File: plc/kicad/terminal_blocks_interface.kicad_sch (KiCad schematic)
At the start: 78 parts, among them CN1 DB128V-5.08-2P-GN-S, CN10 DB128V-5.08-6P-GN-S, CN2 DB128V-5.08-2P-GN-S, CN3 DB128V-5.08-2P-GN-S, CN4 DB128V-5.08-2P-GN-S, CN5 DB128V-5.08-2P-GN-S, CN6 DB128V-5.08-2P-GN-S, CN7 DB128V-5.08-2P-GN-S, CN8 DB128V-5.08-2P-GN-S, CN9 DB128V-5.08-2P-GN-S, Q1 AO3400A, Q2 AO3400A, U1 TCA9535PWR, U2 TPS272C45DRHFR, U3 TPS272C45DRHFR, U4 ADS1115IDGSR, U5 LTV-814S-TA1-A, U6 LTV-814S-TA1-A, U7 LTV-814S-TA1-A, U8 LTV-814S-TA1-A

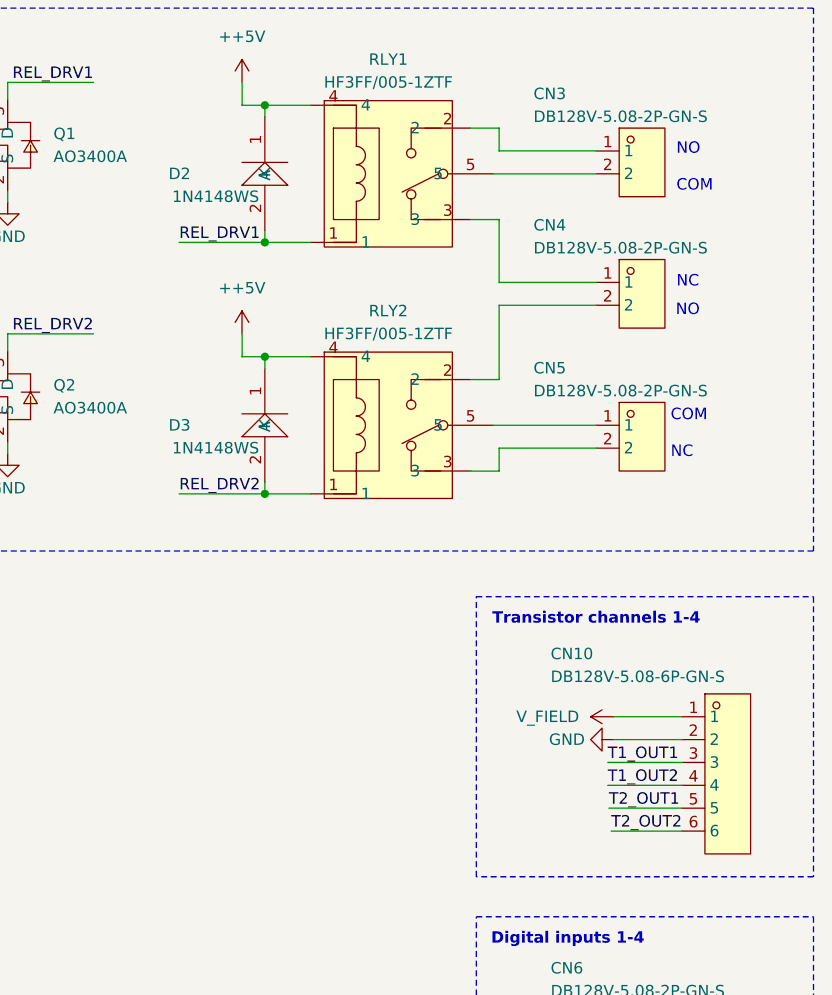
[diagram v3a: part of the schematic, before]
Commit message: Rearranged small PCB placements
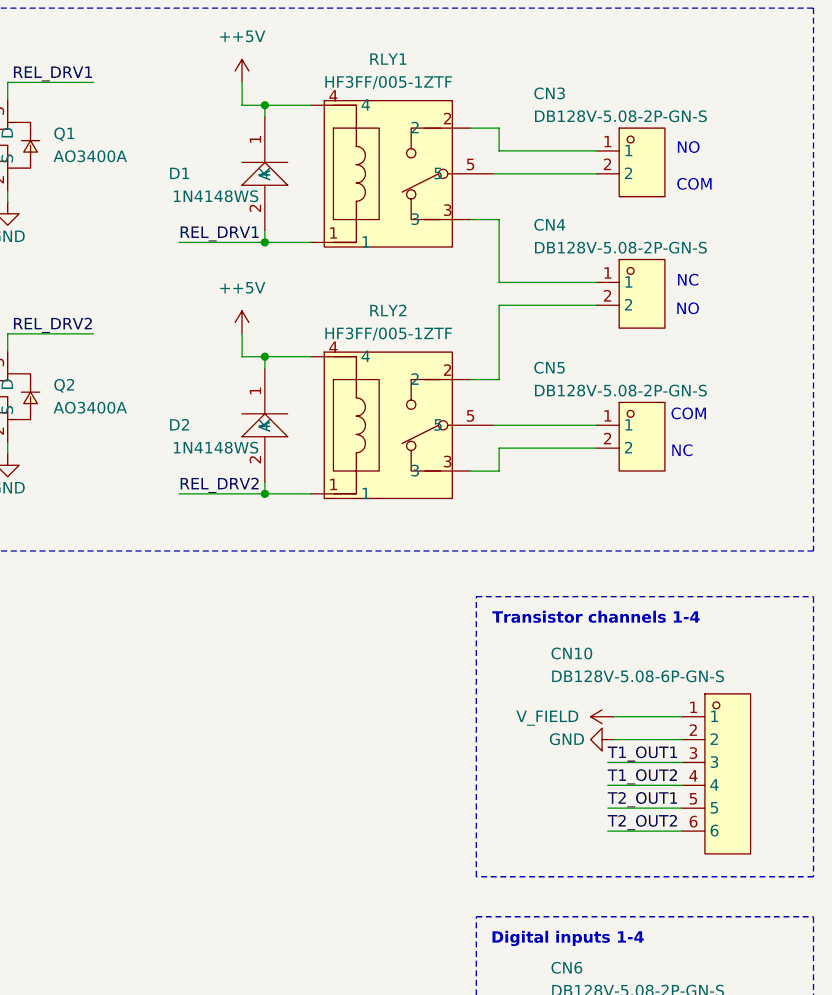
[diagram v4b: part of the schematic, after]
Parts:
- renumbered D2 to D1, D3 to D2
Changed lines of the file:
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@@
 	(wire
 		(pts
-			(xy 376.936 110.49) (xy 384.81 110.49)
+			(xy 376.555 110.49) (xy 384.81 110.49)
 		)
 		(stroke
@@
 	(wire
 		(pts
-			(xy 376.682 107.95) (xy 384.81 107.95)
+			(xy 376.555 107.95) (xy 384.81 107.95)
 		)
 		(stroke
@@
 	)
 	(label "T2_OUT2"
-		(at 376.936 110.49 0)
+		(at 376.555 110.49 0)
 		(effects
 			(font
@@
 	)
 	(label "T2_OUT1"
-		(at 376.682 107.95 0)
+		(at 376.555 107.95 0)
 		(effects
 			(font
@@
 		(in_pos_files yes)
 		(dnp no)
-		(property "Reference" "#PWR068"
+		(property "Reference" "#PWR066"
 			(at 377.19 213.36 0)
 			(hide yes)
@@
 			(project "LibrePLC32"
 				(path "/ef4c1a27-85a3-413a-9f93-a41c4f97eee5/7299de7e-bdc9-4cc1-ab0f-f2b9af304cf6"
-					(reference "#PWR068")
+					(reference "#PWR066")
 					(unit 1)
 				)
@@
 		(dnp no)
 		(fields_autoplaced yes)
-		(property "Reference" "#PWR064"
+		(property "Reference" "#PWR062"
 			(at 335.915 59.055 0)
 			(hide yes)
@@
 			(project "LibrePLC32"
 				(path "/ef4c1a27-85a3-413a-9f93-a41c4f97eee5/7299de7e-bdc9-4cc1-ab0f-f2b9af304cf6"
-					(reference "#PWR064")
+					(reference "#PWR062")
 					(unit 1)
 				)
@@
 		(in_pos_files yes)
 		(dnp no)
-		(property "Reference" "D2"
+		(property "Reference" "D1"
 			(at 330.2 37.465 90)
 			(show_name no)
@@
 			(project "LibrePLC32"
 				(path "/ef4c1a27-85a3-413a-9f93-a41c4f97eee5/7299de7e-bdc9-4cc1-ab0f-f2b9af304cf6"
-					(reference "D2")
+					(reference "D1")
 					(unit 1)
 				)
@@
 		(in_pos_files yes)
 		(dnp no)
-		(property "Reference" "#PWR061"
+		(property "Reference" "#PWR059"
 			(at 309.88 46.99 0)
 			(hide yes)
@@
 			(project "LibrePLC32"
 				(path "/ef4c1a27-85a3-413a-9f93-a41c4f97eee5/7299de7e-bdc9-4cc1-ab0f-f2b9af304cf6"
-					(reference "#PWR061")
+					(reference "#PWR059")
 					(unit 1)
 				)
@@
 		(dnp no)
 		(fields_autoplaced yes)
-		(property "Reference" "#PWR049"
+		(property "Reference" "#PWR047"
 			(at 130.81 264.795 0)
 			(hide yes)
@@
 			(project "LibrePLC32"
 				(path "/ef4c1a27-85a3-413a-9f93-a41c4f97eee5/7299de7e-bdc9-4cc1-ab0f-f2b9af304cf6"
-					(reference "#PWR049")
+					(reference "#PWR047")
 					(unit 1)
 				)
@@
 		(dnp no)
 		(fields_autoplaced yes)
-		(property "Reference" "#PWR063"
+		(property "Reference" "#PWR061"
 			(at 335.915 31.115 0)
 			(hide yes)
@@
 			(project "LibrePLC32"
 				(path "/ef4c1a27-85a3-413a-9f93-a41c4f97eee5/7299de7e-bdc9-4cc1-ab0f-f2b9af304cf6"
-					(reference "#PWR063")
+					(reference "#PWR061")
 					(unit 1)
 				)
@@
 		(dnp no)
 		(fields_autoplaced yes)
-		(property "Reference" "#PWR048"
+		(property "Reference" "#PWR046"
 			(at 130.81 259.715 0)
 			(hide yes)
@@
 			(project "LibrePLC32"
 				(path "/ef4c1a27-85a3-413a-9f93-a41c4f97eee5/7299de7e-bdc9-4cc1-ab0f-f2b9af304cf6"
-					(reference "#PWR048")
+					(reference "#PWR046")
 					(unit 1)
 				)
@@
 		(in_pos_files yes)
 		(dnp no)
-		(property "Reference" "#PWR052"
+		(property "Reference" "#PWR050"
 			(at 216.027 62.992 0)
 			(hide yes)
@@
 			(project "LibrePLC32"
 				(path "/ef4c1a27-85a3-413a-9f93-a41c4f97eee5/7299de7e-bdc9-4cc1-ab0f-f2b9af304cf6"
-					(reference "#PWR052")
+					(reference "#PWR050")
 					(unit 1)
 				)
@@
 		(in_pos_files yes)
 		(dnp no)
-		(property "Reference" "#PWR055"
+		(property "Reference" "#PWR053"
 			(at 227.457 54.737 0)
 			(hide yes)
@@
 			(project "LibrePLC32"
 				(path "/ef4c1a27-85a3-413a-9f93-a41c4f97eee5/7299de7e-bdc9-4cc1-ab0f-f2b9af304cf6"
-					(reference "#PWR055")
+					(reference "#PWR053")
 					(unit 1)
 				)
@@
 		(dnp no)
 		(fields_autoplaced yes)
-		(property "Reference" "#PWR067"
+		(property "Reference" "#PWR065"
 			(at 370.84 100.33 0)
 			(hide yes)
@@
 			(project "LibrePLC32"
 				(path "/ef4c1a27-85a3-413a-9f93-a41c4f97eee5/7299de7e-bdc9-4cc1-ab0f-f2b9af304cf6"
-					(reference "#PWR067")
+					(reference "#PWR065")
 					(unit 1)
 				)
@@
 		(in_pos_files yes)
 		(dnp no)
-		(property "Reference" "#PWR050"
+		(property "Reference" "#PWR048"
 			(at 175.895 264.795 0)
 			(hide yes)
@@
 			(project "LibrePLC32"
 				(path "/ef4c1a27-85a3-413a-9f93-a41c4f97eee5/7299de7e-bdc9-4cc1-ab0f-f2b9af304cf6"
-					(reference "#PWR050")
+					(reference "#PWR048")
 					(unit 1)
 				)
@@
 		(in_pos_files yes)
 		(dnp no)
-		(property "Reference" "#PWR062"
+		(property "Reference" "#PWR060"
 			(at 309.88 74.93 0)
 			(hide yes)
@@
 			(project "LibrePLC32"
 				(path "/ef4c1a27-85a3-413a-9f93-a41c4f97eee5/7299de7e-bdc9-4cc1-ab0f-f2b9af304cf6"
-					(reference "#PWR062")
+					(reference "#PWR060")
 					(unit 1)
 				)
@@
 		(dnp no)
 		(fields_autoplaced yes)
-		(property "Reference" "#PWR066"
+		(property "Reference" "#PWR064"
 			(at 381 97.79 0)
 			(hide yes)
@@
 			(project "LibrePLC32"
 				(path "/ef4c1a27-85a3-413a-9f93-a41c4f97eee5/7299de7e-bdc9-4cc1-ab0f-f2b9af304cf6"
-					(reference "#PWR066")
+					(reference "#PWR064")
 					(unit 1)
 				)
@@
 		(in_pos_files yes)
 		(dnp no)
-		(property "Reference" "#PWR056"
+		(property "Reference" "#PWR054"
 			(at 227.457 83.947 0)
 			(hide yes)
@@
 			(project "LibrePLC32"
 				(path "/ef4c1a27-85a3-413a-9f93-a41c4f97eee5/7299de7e-bdc9-4cc1-ab0f-f2b9af304cf6"
-					(reference "#PWR056")
+					(reference "#PWR054")
 					(unit 1)
 				)
@@
 		(in_pos_files yes)
 		(dnp no)
-		(property "Reference" "#PWR060"
+		(property "Reference" "#PWR058"
 			(at 299.72 79.375 0)
 			(hide yes)
@@
 			(project "LibrePLC32"
 				(path "/ef4c1a27-85a3-413a-9f93-a41c4f97eee5/7299de7e-bdc9-4cc1-ab0f-f2b9af304cf6"
-					(reference "#PWR060")
+					(reference "#PWR058")
 					(unit 1)
 				)
@@
 		(in_pos_files yes)
 		(dnp no)
-		(property "Reference" "#PWR058"
+		(property "Reference" "#PWR056"
 			(at 227.457 141.732 0)
 			(hide yes)
@@
 			(project "LibrePLC32"
 				(path "/ef4c1a27-85a3-413a-9f93-a41c4f97eee5/7299de7e-bdc9-4cc1-ab0f-f2b9af304cf6"
-					(reference "#PWR058")
+					(reference "#PWR056")
 					(unit 1)
 				)
@@
 		(in_pos_files yes)
 		(dnp no)
-		(property "Reference" "#PWR054"
+		(property "Reference" "#PWR052"
 			(at 216.027 120.777 0)
 			(hide yes)
@@
 			(project "LibrePLC32"
 				(path "/ef4c1a27-85a3-413a-9f93-a41c4f97eee5/7299de7e-bdc9-4cc1-ab0f-f2b9af304cf6"
-					(reference "#PWR054")
+					(reference "#PWR052")
 					(unit 1)
 				)
@@
 		(in_pos_files yes)
 		(dnp no)
-		(property "Reference" "#PWR065"
+		(property "Reference" "#PWR063"
 			(at 348.615 223.52 0)
 			(hide yes)
@@
 			(project "LibrePLC32"
 				(path "/ef4c1a27-85a3-413a-9f93-a41c4f97eee5/7299de7e-bdc9-4cc1-ab0f-f2b9af304cf6"
-					(reference "#PWR065")
+					(reference "#PWR063")
 					(unit 1)
 				)
@@
 		(in_pos_files yes)
 		(dnp no)
-		(property "Reference" "#PWR057"
+		(property "Reference" "#PWR055"
 			(at 227.457 111.887 0)
 			(hide yes)
@@
 			(project "LibrePLC32"
 				(path "/ef4c1a27-85a3-413a-9f93-a41c4f97eee5/7299de7e-bdc9-4cc1-ab0f-f2b9af304cf6"
-					(reference "#PWR057")
+					(reference "#PWR055")
 					(unit 1)
 				)
@@
 		(in_pos_files yes)
 		(dnp no)
-		(property "Reference" "#PWR051"
+		(property "Reference" "#PWR049"
 			(at 216.027 33.782 0)
 			(hide yes)
@@
 			(project "LibrePLC32"
 				(path "/ef4c1a27-85a3-413a-9f93-a41c4f97eee5/7299de7e-bdc9-4cc1-ab0f-f2b9af304cf6"
-					(reference "#PWR051")
+					(reference "#PWR049")
 					(unit 1)
 				)
@@
 		(in_pos_files yes)
 		(dnp no)
-		(property "Reference" "#PWR053"
+		(property "Reference" "#PWR051"
 			(at 216.027 90.932 0)
 			(hide yes)
@@
 			(project "LibrePLC32"
 				(path "/ef4c1a27-85a3-413a-9f93-a41c4f97eee5/7299de7e-bdc9-4cc1-ab0f-f2b9af304cf6"
-					(reference "#PWR053")
+					(reference "#PWR051")
 					(unit 1)
 				)
@@
 		(in_pos_files yes)
 		(dnp no)
-		(property "Reference" "#PWR059"
+		(property "Reference" "#PWR057"
 			(at 299.72 51.435 0)
 			(hide yes)
@@
 			(project "LibrePLC32"
 				(path "/ef4c1a27-85a3-413a-9f93-a41c4f97eee5/7299de7e-bdc9-4cc1-ab0f-f2b9af304cf6"
-					(reference "#PWR059")
+					(reference "#PWR057")
 					(unit 1)
 				)
@@
 		(in_pos_files yes)
 		(dnp no)
-		(property "Reference" "D3"
+		(property "Reference" "D2"
 			(at 330.2 65.405 90)
 			(show_name no)
@@
 			(project "LibrePLC32"
 				(path "/ef4c1a27-85a3-413a-9f93-a41c4f97eee5/7299de7e-bdc9-4cc1-ab0f-f2b9af304cf6"
-					(reference "D3")
+					(reference "D2")
 					(unit 1)
 				)

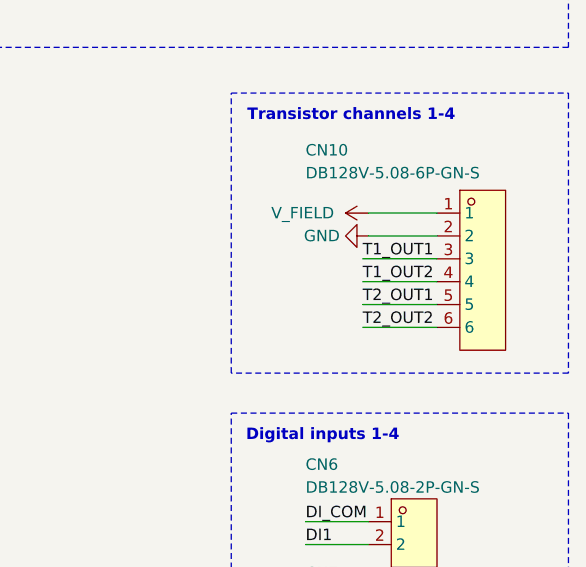
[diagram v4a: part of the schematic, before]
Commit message: TPS272C45 PCB placement
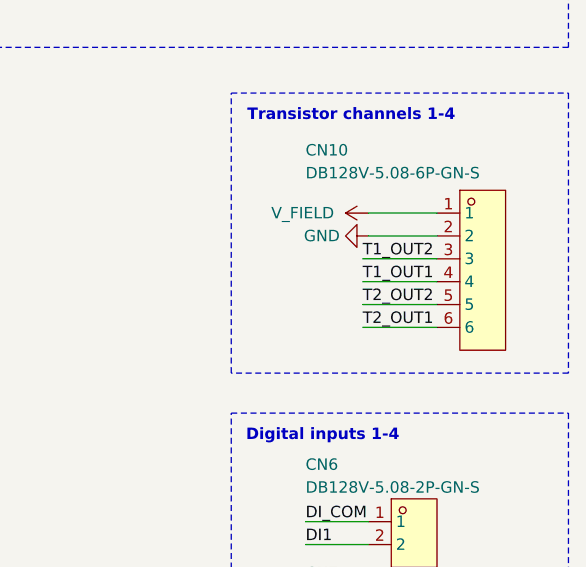
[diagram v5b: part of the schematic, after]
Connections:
- net T1_OUT1: now also CN10.4; no longer CN10.3
- net T1_OUT2: now also CN10.3; no longer CN10.4
- net T2_OUT1: now also CN10.6; no longer CN10.5
- net T2_OUT2: now also CN10.5; no longer CN10.6
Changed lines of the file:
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@@
+		)
+	)
+	(label "T1_OUT2"
+		(at 376.555 102.87 0)
+		(effects
+			(font
+				(size 1.27 1.27)
+			)
+			(justify left bottom)
 		)
 	)
@@
 		)
 	)
-	(label "T1_OUT1"
-		(at 376.555 102.87 0)
-		(effects
-			(font
-				(size 1.27 1.27)
-			)
-			(justify left bottom)
-		)
-	)
-	(label "T2_OUT2"
-		(at 376.555 110.49 0)
-		(effects
-			(font
-				(size 1.27 1.27)
-			)
-			(justify left bottom)
-		)
-	)
 	(label "T2_ADC"
 		(at 50.546 257.429 180)
@@
 		)
 	)
-	(label "T1_OUT2"
-		(at 376.555 105.41 0)
-		(effects
-			(font
-				(size 1.27 1.27)
-			)
-			(justify left bottom)
-		)
-	)
 	(label "T1_FLT2"
 		(at 40.64 55.245 0)
@@
 		)
 	)
-	(label "T2_OUT1"
-		(at 376.555 107.95 0)
-		(effects
-			(font
-				(size 1.27 1.27)
-			)
-			(justify left bottom)
-		)
-	)
 	(label "T1_EN1"
 		(at 31.369 94.107 180)
@@
 		)
 	)
+	(label "T1_OUT1"
+		(at 376.555 105.41 0)
+		(effects
+			(font
+				(size 1.27 1.27)
+			)
+			(justify left bottom)
+		)
+	)
 	(label "T2_FLT1"
 		(at 40.64 57.785 0)
@@
 		)
 	)
+	(label "T2_OUT1"
+		(at 376.555 110.49 0)
+		(effects
+			(font
+				(size 1.27 1.27)
+			)
+			(justify left bottom)
+		)
+	)
 	(label "T1_OUT2"
 		(at 114.173 126.238 180)
@@
 		(effects
 			(font
+				(size 1.27 1.27)
+			)
+			(justify left bottom)
+		)
+	)
+	(label "T2_OUT2"
+		(at 376.555 107.95 0)
+		(effects
+			(font

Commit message: PCB placement updates
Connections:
- net RLY1_NC: now reaches CN3.1
- net RLY1_NC: now also RLY1.3; no longer RLY1.2
- net RLY1_NO: now reaches CN4.1
- net RLY1_NO: now also RLY1.2; no longer RLY1.3
- net RLY2_NC: now reaches RLY2.3
- net RLY2_NC: now also CN4.2; no longer CN5.2
- net RLY2_NO: now reaches RLY2.2
- net RLY2_NO: now also CN5.2; no longer CN4.2
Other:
- note added: "COM NO"
- note added: "NC COM"
- note removed: "COM NC"
- note removed: "NO COM"
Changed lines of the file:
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@@
 		)
 	)
-	(text "NC"
+	(text "NO"
 		(exclude_from_sim no)
 		(at 385.445 49.53 0)
@@
 		)
 	)
-	(text "NO"
+	(text "NC"
 		(exclude_from_sim no)
 		(at 385.445 52.705 0)
@@
 		)
 	)
-	(text "NO\n\nCOM\n"
+	(text "NC\n\nCOM\n"
 		(exclude_from_sim no)
 		(at 384.175 36.83 0)
@@
 		)
 	)
-	(text "\nCOM\n\nNC"
+	(text "\nCOM\n\nNO"
 		(exclude_from_sim no)
 		(at 383.54 65.405 0)
@@
 	(wire
 		(pts
-			(xy 90.043 106.553) (xy 90.043 108.458)
+			(xy 367.03 34.925) (xy 375.285 34.925)
 		)
 		(stroke
@@
 	(wire
 		(pts
-			(xy 364.49 67.945) (xy 375.285 67.945)
+			(xy 90.043 106.553) (xy 90.043 108.458)
 		)
 		(stroke
@@
 	(wire
 		(pts
-			(xy 364.49 34.925) (xy 364.49 32.385)
-		)
-		(stroke
-			(width 0)
-			(type default)
-		)
-	)
-	(wire
-		(pts
 			(xy 68.58 42.545) (xy 77.47 42.545)
 		)
@@
 	(wire
 		(pts
-			(xy 364.49 34.925) (xy 375.285 34.925)
-		)
-		(stroke
-			(width 0)
-			(type default)
-		)
-	)
-	(wire
-		(pts
 			(xy 23.241 232.664) (xy 23.241 231.394)
 		)
@@
 	(wire
 		(pts
-			(xy 361.315 42.545) (xy 364.49 42.545)
+			(xy 361.315 42.545) (xy 368.935 42.545)
 		)
 		(stroke
@@
 	(wire
 		(pts
-			(xy 364.49 32.385) (xy 361.315 32.385)
+			(xy 368.935 32.385) (xy 361.315 32.385)
 		)
 		(stroke
@@
 	(wire
 		(pts
-			(xy 364.49 49.53) (xy 375.285 49.53)
+			(xy 367.03 49.53) (xy 375.285 49.53)
 		)
 		(stroke
@@
 	(wire
 		(pts
+			(xy 367.03 67.945) (xy 375.285 67.945)
+		)
+		(stroke
+			(width 0)
+			(type default)
+		)
+	)
+	(wire
+		(pts
 			(xy 181.102 69.342) (xy 182.372 69.342)
 		)
@@
 	(wire
 		(pts
-			(xy 364.49 60.325) (xy 364.49 52.07)
-		)
-		(stroke
-			(width 0)
-			(type default)
-		)
-	)
-	(wire
-		(pts
 			(xy 354.33 227.965) (xy 342.9 227.965)
 		)
@@
 	(wire
 		(pts
-			(xy 364.49 52.07) (xy 375.285 52.07)
-		)
-		(stroke
-			(width 0)
-			(type default)
-		)
-	)
-	(wire
-		(pts
 			(xy 342.9 207.645) (xy 342.9 205.105)
 		)
@@
 	(wire
 		(pts
-			(xy 364.49 60.325) (xy 361.315 60.325)
+			(xy 369.57 60.325) (xy 361.315 60.325)
 		)
 		(stroke
@@
 	(wire
 		(pts
-			(xy 364.49 70.485) (xy 364.49 67.945)
-		)
-		(stroke
-			(width 0)
-			(type default)
-		)
-	)
-	(wire
-		(pts
 			(xy 76.2 211.455) (xy 74.93 211.455)
 		)
@@
 	(wire
 		(pts
-			(xy 364.49 42.545) (xy 364.49 49.53)
-		)
-		(stroke
-			(width 0)
-			(type default)
-		)
-	)
-	(wire
-		(pts
 			(xy 66.548 121.158) (xy 76.073 121.158)
 		)
@@
 	(wire
 		(pts
-			(xy 361.315 70.485) (xy 364.49 70.485)
+			(xy 361.315 70.485) (xy 369.57 70.485)
 		)
 		(stroke
@@
 	(wire
 		(pts
+			(xy 367.03 52.07) (xy 375.285 52.07)
+		)
+		(stroke
+			(width 0)
+			(type default)
+		)
+	)
+	(wire
+		(pts
 			(xy 66.675 234.315) (xy 76.2 234.315)
 		)
@@
 		)
 	)
+	(label "RLY2_NC"
+		(at 367.03 52.07 0)
+		(effects
+			(font
+				(size 1.27 1.27)
+			)
+			(justify left bottom)
+		)
+	)
 	(label "T1_FLT1"
 		(at 58.674 127.762 180)
@@
 		)
 	)
+	(label "RLY1_NC"
+		(at 368.935 42.545 180)
+		(effects
+			(font
+				(size 1.27 1.27)
+			)
+			(justify right bottom)
+		)
+	)
 	(label "T2_ADC"
 		(at 50.546 257.429 180)
@@
 		)
 	)
+	(label "RLY1_NO"
+		(at 367.03 49.53 0)
+		(effects
+			(font
+				(size 1.27 1.27)
+			)
+			(justify left bottom)
+		)
+	)
 	(label "T2_SNS"
 		(at 20.701 257.429 0)
@@
 		)
 	)
+	(label "RLY2_NO"
+		(at 367.03 67.945 0)
+		(effects
+			(font
+				(size 1.27 1.27)
+			)
+			(justify left bottom)
+		)
+	)
 	(label "T1_EN1"
 		(at 31.369 94.107 180)
@@
 		)
 	)
+	(label "RLY1_NO"
+		(at 368.935 32.385 180)
+		(effects
+			(font
+				(size 1.27 1.27)
+			)
+			(justify right bottom)
+		)
+	)
 	(label "MCU_DI1"
 		(at 236.347 36.957 180)
@@
 		)
 	)
+	(label "RLY2_NO"
+		(at 369.57 60.325 180)
+		(effects
+			(font
+				(size 1.27 1.27)
+			)
+			(justify right bottom)
+		)
+	)
 	(label "T2_FLT2"
 		(at 66.675 226.695 0)
@@
 		)
 	)
+	(label "RLY2_NC"
+		(at 369.57 70.485 180)
+		(effects
+			(font
+				(size 1.27 1.27)
+			)
+			(justify right bottom)
+		)
+	)
 	(label "T2_SEL"
 		(at 66.675 239.395 0)
@@
 		)
 	)
+	(label "RLY1_NC"
+		(at 367.03 34.925 0)
+		(effects
+			(font
+				(size 1.27 1.27)
+			)
+			(justify left bottom)
+		)
+	)
 	(label "T2_FLT1"
 		(at 58.801 225.679 180)
@@
 		(dnp no)
 		(property "Reference" "CN5"
-			(at 368.3 59.055 0)
+			(at 372.745 59.055 0)
 			(show_name no)
 			(do_not_autoplace no)
@@
 		)
 		(property "Value" "DB128V-5.08-2P-GN-S"
-			(at 368.3 61.595 0)
+			(at 372.745 61.595 0)
 			(show_name no)
 			(do_not_autoplace no)
@@
 		(dnp no)
 		(property "Reference" "CN4"
-			(at 368.3 43.18 0)
+			(at 372.745 43.18 0)
 			(show_name no)
 			(do_not_autoplace no)
@@
 		)
 		(property "Value" "DB128V-5.08-2P-GN-S"
-			(at 368.3 45.72 0)
+			(at 372.745 45.72 0)
 			(show_name no)
 			(do_not_autoplace no)
@@
 		(dnp no)
 		(property "Reference" "CN3"
-			(at 368.3 28.575 0)
+			(at 372.745 28.575 0)
 			(show_name no)
 			(do_not_autoplace no)
@@
 		)
 		(property "Value" "DB128V-5.08-2P-GN-S"
-			(at 368.3 31.115 0)
+			(at 372.745 31.115 0)
 			(show_name no)
 			(do_not_autoplace no)
